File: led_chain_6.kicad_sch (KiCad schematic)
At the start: 0 parts

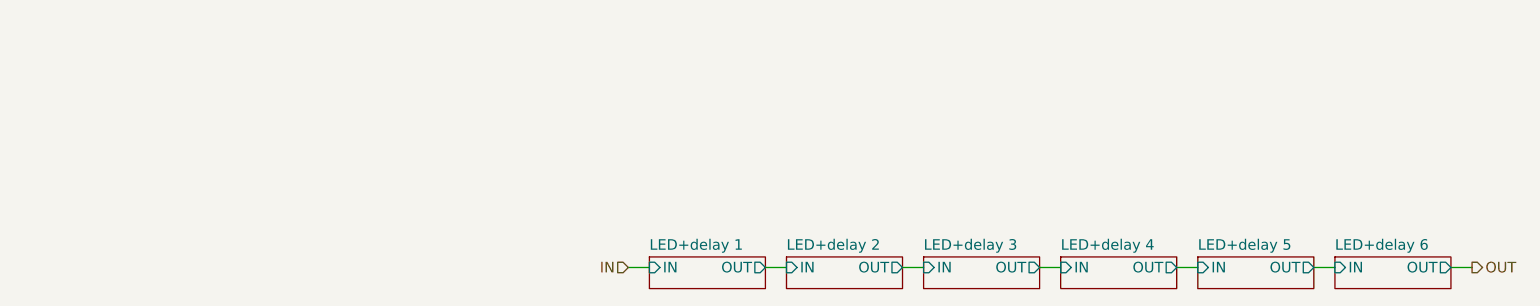
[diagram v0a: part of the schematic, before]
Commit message: pcb-text plugin applied, next step is to write a replicate layout plugin that actually works
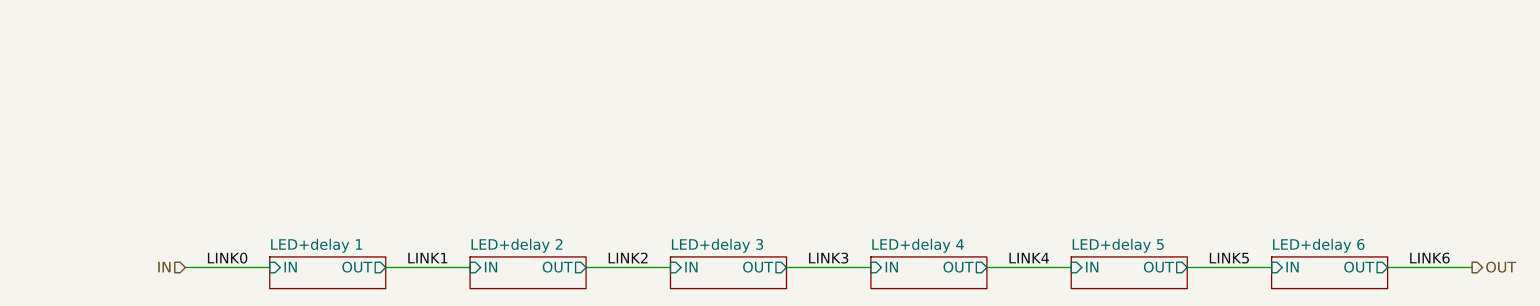
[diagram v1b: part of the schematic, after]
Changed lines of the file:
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@@
 (kicad_sch (version 20211123) (generator eeschema)
   (paper "A5")
-  (wire (pts (xy 186.69 95.25) (xy 189.23 95.25))
+  (wire (pts (xy 179.07 95.25) (xy 189.23 95.25))
     (stroke (width 0) (type default) (color 0 0 0 0))
   )
-  (wire (pts (xy 137.16 95.25) (xy 139.7 95.25))
+  (wire (pts (xy 106.68 95.25) (xy 116.84 95.25))
     (stroke (width 0) (type default) (color 0 0 0 0))
   )
-  (wire (pts (xy 120.65 95.25) (xy 123.19 95.25))
+  (wire (pts (xy 82.55 95.25) (xy 92.71 95.25))
     (stroke (width 0) (type default) (color 0 0 0 0))
   )
-  (wire (pts (xy 153.67 95.25) (xy 156.21 95.25))
+  (wire (pts (xy 130.81 95.25) (xy 140.97 95.25))
     (stroke (width 0) (type default) (color 0 0 0 0))
   )
-  (wire (pts (xy 104.14 95.25) (xy 106.68 95.25))
+  (wire (pts (xy 58.42 95.25) (xy 68.58 95.25))
     (stroke (width 0) (type default) (color 0 0 0 0))
   )
-  (wire (pts (xy 170.18 95.25) (xy 172.72 95.25))
+  (wire (pts (xy 154.94 95.25) (xy 165.1 95.25))
     (stroke (width 0) (type default) (color 0 0 0 0))
   )
-  (wire (pts (xy 87.63 95.25) (xy 90.17 95.25))
+  (wire (pts (xy 34.29 95.25) (xy 44.45 95.25))
     (stroke (width 0) (type default) (color 0 0 0 0))
   )
@@
     (effects (font (size 2.54 2.54) (thickness 0.508) bold) (justify left bottom))
   )
+  (label "LINK6" (at 181.61 95.25 0)
+    (effects (font (size 1.27 1.27)) (justify left bottom))
+  )
+  (label "LINK1" (at 60.96 95.25 0)
+    (effects (font (size 1.27 1.27)) (justify left bottom))
+  )
+  (label "LINK4" (at 133.35 95.25 0)
+    (effects (font (size 1.27 1.27)) (justify left bottom))
+  )
+  (label "LINK3" (at 109.22 95.25 0)
+    (effects (font (size 1.27 1.27)) (justify left bottom))
+  )
+  (label "LINK2" (at 85.09 95.25 0)
+    (effects (font (size 1.27 1.27)) (justify left bottom))
+  )
+  (label "LINK0" (at 36.83 95.25 0)
+    (effects (font (size 1.27 1.27)) (justify left bottom))
+  )
+  (label "LINK5" (at 157.48 95.25 0)
+    (effects (font (size 1.27 1.27)) (justify left bottom))
+  )
   (hierarchical_label "OUT" (shape output) (at 189.23 95.25 0)
     (effects (font (size 1.27 1.27)) (justify left))
   )
-  (hierarchical_label "IN" (shape input) (at 87.63 95.25 180)
+  (hierarchical_label "IN" (shape input) (at 34.29 95.25 180)
     (effects (font (size 1.27 1.27)) (justify right))
   )
-  (sheet (at 172.72 93.98) (size 13.97 3.81) (fields_autoplaced)
+  (sheet (at 165.1 93.98) (size 13.97 3.81) (fields_autoplaced)
     (stroke (width 0.1524) (type solid) (color 0 0 0 0))
     (fill (color 0 0 0 0.0000))
-    (property "Sheet name" "LED+delay 6" (id 0) (at 172.72 93.2684 0)
+    (property "Sheet name" "LED+delay 6" (id 0) (at 165.1 93.2684 0)
       (effects (font (size 1.27 1.27)) (justify left bottom))
     )
-    (property "Sheet file" "led_chain_delay_link.kicad_sch" (id 1) (at 172.72 98.3746 0)
+    (property "Sheet file" "led_chain_delay_link.kicad_sch" (id 1) (at 165.1 98.3746 0)
       (effects (font (size 1.27 1.27)) (justify left top) hide)
     )
-    (pin "IN" input (at 172.72 95.25 180)
+    (pin "IN" input (at 165.1 95.25 180)
       (effects (font (size 1.27 1.27)) (justify left))
     )
-    (pin "OUT" output (at 186.69 95.25 0)
+    (pin "OUT" output (at 179.07 95.25 0)
       (effects (font (size 1.27 1.27)) (justify right))
     )
   )
-  (sheet (at 123.19 93.98) (size 13.97 3.81) (fields_autoplaced)
+  (sheet (at 92.71 93.98) (size 13.97 3.81) (fields_autoplaced)
     (stroke (width 0.1524) (type solid) (color 0 0 0 0))
     (fill (color 0 0 0 0.0000))
-    (property "Sheet name" "LED+delay 3" (id 0) (at 123.19 93.2684 0)
+    (property "Sheet name" "LED+delay 3" (id 0) (at 92.71 93.2684 0)
       (effects (font (size 1.27 1.27)) (justify left bottom))
     )
-    (property "Sheet file" "led_chain_delay_link.kicad_sch" (id 1) (at 123.19 98.3746 0)
+    (property "Sheet file" "led_chain_delay_link.kicad_sch" (id 1) (at 92.71 98.3746 0)
       (effects (font (size 1.27 1.27)) (justify left top) hide)
     )
-    (pin "IN" input (at 123.19 95.25 180)
+    (pin "IN" input (at 92.71 95.25 180)
       (effects (font (size 1.27 1.27)) (justify left))
     )
-    (pin "OUT" output (at 137.16 95.25 0)
+    (pin "OUT" output (at 106.68 95.25 0)
       (effects (font (size 1.27 1.27)) (justify right))
     )
   )
-  (sheet (at 139.7 93.98) (size 13.97 3.81) (fields_autoplaced)
+  (sheet (at 116.84 93.98) (size 13.97 3.81) (fields_autoplaced)
     (stroke (width 0.1524) (type solid) (color 0 0 0 0))
     (fill (color 0 0 0 0.0000))
-    (property "Sheet name" "LED+delay 4" (id 0) (at 139.7 93.2684 0)
+    (property "Sheet name" "LED+delay 4" (id 0) (at 116.84 93.2684 0)
       (effects (font (size 1.27 1.27)) (justify left bottom))
     )
-    (property "Sheet file" "led_chain_delay_link.kicad_sch" (id 1) (at 139.7 98.3746 0)
+    (property "Sheet file" "led_chain_delay_link.kicad_sch" (id 1) (at 116.84 98.3746 0)
       (effects (font (size 1.27 1.27)) (justify left top) hide)
     )
-    (pin "IN" input (at 139.7 95.25 180)
+    (pin "IN" input (at 116.84 95.25 180)
       (effects (font (size 1.27 1.27)) (justify left))
     )
-    (pin "OUT" output (at 153.67 95.25 0)
+    (pin "OUT" output (at 130.81 95.25 0)
       (effects (font (size 1.27 1.27)) (justify right))
     )
   )
-  (sheet (at 106.68 93.98) (size 13.97 3.81) (fields_autoplaced)
+  (sheet (at 68.58 93.98) (size 13.97 3.81) (fields_autoplaced)
     (stroke (width 0.1524) (type solid) (color 0 0 0 0))
     (fill (color 0 0 0 0.0000))
-    (property "Sheet name" "LED+delay 2" (id 0) (at 106.68 93.2684 0)
+    (property "Sheet name" "LED+delay 2" (id 0) (at 68.58 93.2684 0)
       (effects (font (size 1.27 1.27)) (justify left bottom))
     )
-    (property "Sheet file" "led_chain_delay_link.kicad_sch" (id 1) (at 106.68 98.3746 0)
+    (property "Sheet file" "led_chain_delay_link.kicad_sch" (id 1) (at 68.58 98.3746 0)
       (effects (font (size 1.27 1.27)) (justify left top) hide)
     )
-    (pin "IN" input (at 106.68 95.25 180)
+    (pin "IN" input (at 68.58 95.25 180)
       (effects (font (size 1.27 1.27)) (justify left))
     )
-    (pin "OUT" output (at 120.65 95.25 0)
+    (pin "OUT" output (at 82.55 95.25 0)
       (effects (font (size 1.27 1.27)) (justify right))
     )
   )
-  (sheet (at 156.21 93.98) (size 13.97 3.81) (fields_autoplaced)
+  (sheet (at 140.97 93.98) (size 13.97 3.81) (fields_autoplaced)
     (stroke (width 0.1524) (type solid) (color 0 0 0 0))
     (fill (color 0 0 0 0.0000))
-    (property "Sheet name" "LED+delay 5" (id 0) (at 156.21 93.2684 0)
+    (property "Sheet name" "LED+delay 5" (id 0) (at 140.97 93.2684 0)
       (effects (font (size 1.27 1.27)) (justify left bottom))
     )
-    (property "Sheet file" "led_chain_delay_link.kicad_sch" (id 1) (at 156.21 98.3746 0)
+    (property "Sheet file" "led_chain_delay_link.kicad_sch" (id 1) (at 140.97 98.3746 0)
       (effects (font (size 1.27 1.27)) (justify left top) hide)
     )
-    (pin "IN" input (at 156.21 95.25 180)
+    (pin "IN" input (at 140.97 95.25 180)
       (effects (font (size 1.27 1.27)) (justify left))
     )
-    (pin "OUT" output (at 170.18 95.25 0)
+    (pin "OUT" output (at 154.94 95.25 0)
       (effects (font (size 1.27 1.27)) (justify right))
     )
   )
-  (sheet (at 90.17 93.98) (size 13.97 3.81) (fields_autoplaced)
+  (sheet (at 44.45 93.98) (size 13.97 3.81) (fields_autoplaced)
     (stroke (width 0.1524) (type solid) (color 0 0 0 0))
     (fill (color 0 0 0 0.0000))
-    (property "Sheet name" "LED+delay 1" (id 0) (at 90.17 93.2684 0)
+    (property "Sheet name" "LED+delay 1" (id 0) (at 44.45 93.2684 0)
       (effects (font (size 1.27 1.27)) (justify left bottom))
     )
-    (property "Sheet file" "led_chain_delay_link.kicad_sch" (id 1) (at 90.17 98.3746 0)
+    (property "Sheet file" "led_chain_delay_link.kicad_sch" (id 1) (at 44.45 98.3746 0)
       (effects (font (size 1.27 1.27)) (justify left top) hide)
     )
-    (pin "IN" input (at 90.17 95.25 180)
+    (pin "IN" input (at 44.45 95.25 180)
       (effects (font (size 1.27 1.27)) (justify left))
     )
-    (pin "OUT" output (at 104.14 95.25 0)
+    (pin "OUT" output (at 58.42 95.25 0)
       (effects (font (size 1.27 1.27)) (justify right))
     )
